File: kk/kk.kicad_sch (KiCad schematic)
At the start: 2 parts, among them J1 Conn_01x02_Pin, J2 Conn_01x02_Pin

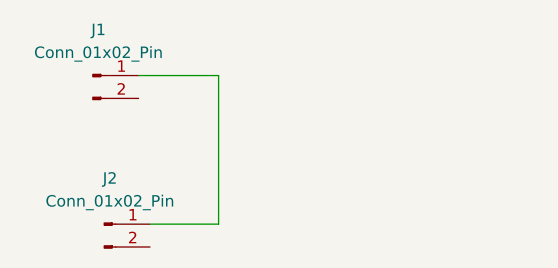
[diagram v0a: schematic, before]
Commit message: less wires.
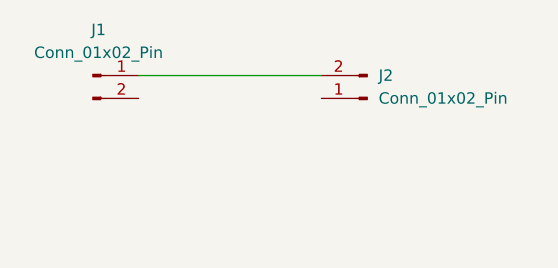
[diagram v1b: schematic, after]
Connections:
- net at J2.1 (Pin_1): no longer J1.1 (Pin_1)
- net at J2.2 (Pin_2): now also J1.1 (Pin_1)
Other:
- moved on the sheet: J2
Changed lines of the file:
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@@
 	(wire
 		(pts
-			(xy 107.95 64.77) (xy 107.95 81.28)
-		)
-		(stroke
-			(width 0)
-			(type default)
-		)
-	)
-	(wire
-		(pts
-			(xy 99.06 64.77) (xy 107.95 64.77)
-		)
-		(stroke
-			(width 0)
-			(type default)
-		)
-	)
-	(wire
-		(pts
-			(xy 107.95 81.28) (xy 100.33 81.28)
+			(xy 99.06 64.77) (xy 119.38 64.77)
 		)
 		(stroke
@@
 	(symbol
 		(lib_id "Connector:Conn_01x02_Pin")
-		(at 95.25 81.28 0)
+		(at 124.46 67.31 180)
 		(unit 1)
 		(exclude_from_sim no)
@@
 		(fields_autoplaced yes)
 		(property "Reference" "J2"
-			(at 95.885 76.2 0)
+			(at 125.73 64.7699 0)
 			(effects
 				(font
 					(size 1.27 1.27)
 				)
+				(justify right)
 			)
 		)
 		(property "Value" "Conn_01x02_Pin"
-			(at 95.885 78.74 0)
+			(at 125.73 67.3099 0)
 			(effects
 				(font
 					(size 1.27 1.27)
 				)
+				(justify right)
 			)
 		)
 		(property "Footprint" ""
-			(at 95.25 81.28 0)
+			(at 124.46 67.31 0)
 			(effects
 				(font
@@
 		)
 		(property "Datasheet" "~"
-			(at 95.25 81.28 0)
+			(at 124.46 67.31 0)
 			(effects
 				(font
@@
 		)
 		(property "Description" "Generic connector, single row, 01x02, script generated"
-			(at 95.25 81.28 0)
+			(at 124.46 67.31 0)
 			(effects
 				(font
